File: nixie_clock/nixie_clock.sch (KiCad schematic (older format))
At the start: 1 part

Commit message: minor cleanups
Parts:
- gave numbers to parts that had none: 1
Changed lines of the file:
@@
 $EndSheet
 $Comp
-L GND #PWR?
+L GND #PWR01
 U 1 1 590D8C11
-P 3300 3050
-F 0 "#PWR?" H 3300 2800 50  0001 C CNN
-F 1 "GND" H 3300 2900 50  0000 C CNN
-F 2 "" H 3300 3050 50  0000 C CNN
-F 3 "" H 3300 3050 50  0000 C CNN
-	1    3300 3050
-	1    0    0    -1
-$EndComp
-$Comp
-L +5V #PWR?
+P 3300 3100
+F 0 "#PWR01" H 3300 2850 50  0001 C CNN
+F 1 "GND" H 3300 2950 50  0000 C CNN
+F 2 "" H 3300 3100 50  0000 C CNN
+F 3 "" H 3300 3100 50  0000 C CNN
+	1    3300 3100
+	1    0    0    -1
+$EndComp
+$Comp
+L +5V #PWR02
 U 1 1 590D8C5B
 P 3000 2700
-F 0 "#PWR?" H 3000 2550 50  0001 C CNN
+F 0 "#PWR02" H 3000 2550 50  0001 C CNN
 F 1 "+5V" H 3000 2840 50  0000 C CNN
 F 2 "" H 3000 2700 50  0000 C CNN
@@
 $EndComp
 $Comp
-L +220V #PWR?
+L +220V #PWR03
 U 1 1 5910C9E4
 P 3300 2600
-F 0 "#PWR?" H 3300 2450 50  0001 C CNN
+F 0 "#PWR03" H 3300 2450 50  0001 C CNN
 F 1 "+220V" H 3300 2740 50  0000 C CNN
 F 2 "" H 3300 2600 50  0000 C CNN
@@
 $EndSheet
 $Comp
-L +220V #PWR?
+L +220V #PWR04
 U 1 1 591129F5
 P 3300 1550
-F 0 "#PWR?" H 3300 1400 50  0001 C CNN
+F 0 "#PWR04" H 3300 1400 50  0001 C CNN
 F 1 "+220V" H 3300 1690 50  0000 C CNN
 F 2 "" H 3300 1550 50  0000 C CNN
@@
 $EndComp
 $Comp
-L +5V #PWR?
+L +5V #PWR05
 U 1 1 59112AB7
 P 2950 1700
-F 0 "#PWR?" H 2950 1550 50  0001 C CNN
+F 0 "#PWR05" H 2950 1550 50  0001 C CNN
 F 1 "+5V" H 2950 1840 50  0000 C CNN
 F 2 "" H 2950 1700 50  0000 C CNN
@@
 $EndComp
 $Comp
-L GND #PWR?
+L GND #PWR06
 U 1 1 59112B79
-P 3300 2000
-F 0 "#PWR?" H 3300 1750 50  0001 C CNN
-F 1 "GND" H 3300 1850 50  0000 C CNN
-F 2 "" H 3300 2000 50  0000 C CNN
-F 3 "" H 3300 2000 50  0000 C CNN
-	1    3300 2000
-	1    0    0    -1
-$EndComp
-$Comp
-L GND #PWR?
+P 3300 2050
+F 0 "#PWR06" H 3300 1800 50  0001 C CNN
+F 1 "GND" H 3300 1900 50  0000 C CNN
+F 2 "" H 3300 2050 50  0000 C CNN
+F 3 "" H 3300 2050 50  0000 C CNN
+	1    3300 2050
+	1    0    0    -1
+$EndComp
+$Comp
+L GND #PWR07
 U 1 1 59112C3B
 P 3300 4150
-F 0 "#PWR?" H 3300 3900 50  0001 C CNN
+F 0 "#PWR07" H 3300 3900 50  0001 C CNN
 F 1 "GND" H 3300 4000 50  0000 C CNN
 F 2 "" H 3300 4150 50  0000 C CNN
@@
 $EndComp
 $Comp
-L GND #PWR?
+L GND #PWR08
 U 1 1 59113990
 P 3100 5300
-F 0 "#PWR?" H 3100 5050 50  0001 C CNN
+F 0 "#PWR08" H 3100 5050 50  0001 C CNN
 F 1 "GND" H 3100 5150 50  0000 C CNN
 F 2 "" H 3100 5300 50  0000 C CNN
@@
 $EndComp
 $Comp
-L GND #PWR?
+L GND #PWR09
 U 1 1 59113A52
 P 3050 7150
-F 0 "#PWR?" H 3050 6900 50  0001 C CNN
+F 0 "#PWR09" H 3050 6900 50  0001 C CNN
 F 1 "GND" H 3050 7000 50  0000 C CNN
 F 2 "" H 3050 7150 50  0000 C CNN
@@
 $EndComp
 $Comp
-L +5V #PWR?
+L +5V #PWR010
 U 1 1 591147FE
 P 3000 3750
-F 0 "#PWR?" H 3000 3600 50  0001 C CNN
+F 0 "#PWR010" H 3000 3600 50  0001 C CNN
 F 1 "+5V" H 3000 3890 50  0000 C CNN
 F 2 "" H 3000 3750 50  0000 C CNN
@@
 $EndComp
 $Comp
-L +5V #PWR?
+L +5V #PWR011
 U 1 1 591148C0
 P 3000 4850
-F 0 "#PWR?" H 3000 4700 50  0001 C CNN
+F 0 "#PWR011" H 3000 4700 50  0001 C CNN
 F 1 "+5V" H 3000 4990 50  0000 C CNN
 F 2 "" H 3000 4850 50  0000 C CNN
@@
 $EndComp
 $Comp
-L +5V #PWR?
+L +5V #PWR012
 U 1 1 59115615
 P 3000 5850
-F 0 "#PWR?" H 3000 5700 50  0001 C CNN
+F 0 "#PWR012" H 3000 5700 50  0001 C CNN
 F 1 "+5V" H 3000 5990 50  0000 C CNN
 F 2 "" H 3000 5850 50  0000 C CNN
@@
 $EndComp
 $Comp
-L +5V #PWR?
+L +5V #PWR013
 U 1 1 591156D7
 P 3050 6900
-F 0 "#PWR?" H 3050 6750 50  0001 C CNN
+F 0 "#PWR013" H 3050 6750 50  0001 C CNN
 F 1 "+5V" H 3050 7040 50  0000 C CNN
 F 2 "" H 3050 6900 50  0000 C CNN
@@
 $EndComp
 $Comp
-L +220V #PWR?
+L +220V #PWR014
 U 1 1 591174D3
 P 3350 3600
-F 0 "#PWR?" H 3350 3450 50  0001 C CNN
+F 0 "#PWR014" H 3350 3450 50  0001 C CNN
 F 1 "+220V" H 3350 3740 50  0000 C CNN
 F 2 "" H 3350 3600 50  0000 C CNN
@@
 $EndComp
 $Comp
-L +220V #PWR?
+L +220V #PWR015
 U 1 1 59117595
 P 3000 4550
-F 0 "#PWR?" H 3000 4400 50  0001 C CNN
+F 0 "#PWR015" H 3000 4400 50  0001 C CNN
 F 1 "+220V" H 3000 4690 50  0000 C CNN
 F 2 "" H 3000 4550 50  0000 C CNN
@@
 $EndComp
 $Comp
-L +220V #PWR?
+L +220V #PWR016
 U 1 1 59118341
 P 2750 5650
-F 0 "#PWR?" H 2750 5500 50  0001 C CNN
+F 0 "#PWR016" H 2750 5500 50  0001 C CNN
 F 1 "+220V" H 2750 5790 50  0000 C CNN
 F 2 "" H 2750 5650 50  0000 C CNN
@@
 $EndComp
 $Comp
-L +220V #PWR?
+L +220V #PWR017
 U 1 1 59118403
 P 2800 6650
-F 0 "#PWR?" H 2800 6500 50  0001 C CNN
+F 0 "#PWR017" H 2800 6500 50  0001 C CNN
 F 1 "+220V" H 2800 6790 50  0000 C CNN
 F 2 "" H 2800 6650 50  0000 C CNN
@@
 	3450 6650 2800 6650
 $Comp
-L GND #PWR?
+L GND #PWR018
 U 1 1 5911B892
-P 3300 6150
-F 0 "#PWR?" H 3300 5900 50  0001 C CNN
-F 1 "GND" H 3300 6000 50  0000 C CNN
-F 2 "" H 3300 6150 50  0000 C CNN
-F 3 "" H 3300 6150 50  0000 C CNN
-	1    3300 6150
+P 3300 6200
+F 0 "#PWR018" H 3300 5950 50  0001 C CNN
+F 1 "GND" H 3300 6050 50  0000 C CNN
+F 2 "" H 3300 6200 50  0000 C CNN
+F 3 "" H 3300 6200 50  0000 C CNN
+	1    3300 6200
 	1    0    0    -1
 $EndComp
@@
 	3450 6150 3300 6150
 $Comp
-L CONN_01X04 P?
+L CONN_01X04 P1
 U 1 1 5911C866
 P 1850 1750
-F 0 "P?" H 1850 2000 50  0000 C CNN
+F 0 "P1" H 1850 2000 50  0000 C CNN
 F 1 "CONN_01X04" V 1950 1750 50  0000 C CNN
 F 2 "" H 1850 1750 50  0000 C CNN
@@
 $EndComp
 $Comp
-L GND #PWR?
+L GND #PWR019
 U 1 1 5910DDAF
 P 1650 2000
-F 0 "#PWR?" H 1650 1750 50  0001 C CNN
+F 0 "#PWR019" H 1650 1750 50  0001 C CNN
 F 1 "GND" H 1650 1850 50  0000 C CNN
 F 2 "" H 1650 2000 50  0000 C CNN
@@
 $EndComp
 $Comp
-L +5V #PWR?
+L +5V #PWR020
 U 1 1 5910DE73
 P 1500 1700
-F 0 "#PWR?" H 1500 1550 50  0001 C CNN
+F 0 "#PWR020" H 1500 1550 50  0001 C CNN
 F 1 "+5V" H 1500 1840 50  0000 C CNN
 F 2 "" H 1500 1700 50  0000 C CNN
@@
 $EndComp
 $Comp
-L +220V #PWR?
+L +220V #PWR021
 U 1 1 5910DF37
 P 1650 1450
-F 0 "#PWR?" H 1650 1300 50  0001 C CNN
+F 0 "#PWR021" H 1650 1300 50  0001 C CNN
 F 1 "+220V" H 1650 1590 50  0000 C CNN
 F 2 "" H 1650 1450 50  0000 C CNN
@@
 Wire Wire Line
 	2700 1850 3450 1850
+$Comp
+L PWR_FLAG #FLG022
+U 1 1 5913737C
+P 1150 1700
+F 0 "#FLG022" H 1150 1795 50  0001 C CNN
+F 1 "PWR_FLAG" H 1150 1880 50  0000 C CNN
+F 2 "" H 1150 1700 50  0000 C CNN
+F 3 "" H 1150 1700 50  0000 C CNN
+	1    1150 1700
+	1    0    0    -1
+$EndComp
+$Comp
+L PWR_FLAG #FLG023
+U 1 1 59137440
+P 1150 1400
+F 0 "#FLG023" H 1150 1495 50  0001 C CNN
+F 1 "PWR_FLAG" H 1150 1580 50  0000 C CNN
+F 2 "" H 1150 1400 50  0000 C CNN
+F 3 "" H 1150 1400 50  0000 C CNN
+	1    1150 1400
+	1    0    0    -1
+$EndComp
+Wire Wire Line
+	1150 1400 1500 1400
+Wire Wire Line
+	1500 1400 1500 1500
+Wire Wire Line
+	1500 1500 1650 1500
+Connection ~ 1650 1500
+Wire Wire Line
+	1150 1700 1150 1750
+Wire Wire Line
+	1150 1750 1550 1750
+Wire Wire Line
+	1550 1750 1550 1700
+Connection ~ 1550 1700
+Wire Wire Line
+	3300 2050 3300 2000
+Wire Wire Line
+	3300 3050 3300 3100
+Wire Wire Line
+	3300 6150 3300 6200
+$Comp
+L PWR_FLAG #FLG024
+U 1 1 5914A430
+P 1150 2000
+F 0 "#FLG024" H 1150 2095 50  0001 C CNN
+F 1 "PWR_FLAG" H 1150 2180 50  0000 C CNN
+F 2 "" H 1150 2000 50  0000 C CNN
+F 3 "" H 1150 2000 50  0000 C CNN
+	1    1150 2000
+	1    0    0    -1
+$EndComp
+Wire Wire Line
+	1650 2000 1150 2000
 $EndSCHEMATC

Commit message: Footprint associations
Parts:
- P1: footprint (none) -> Pin_Headers:Pin_Header_Straight_1x04_Pitch2.54mm
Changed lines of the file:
@@
 F 0 "P1" H 1850 2000 50  0000 C CNN
 F 1 "CONN_01X04" V 1950 1750 50  0000 C CNN
-F 2 "" H 1850 1750 50  0000 C CNN
+F 2 "Pin_Headers:Pin_Header_Straight_1x04_Pitch2.54mm" H 1850 1750 50  0001 C CNN
 F 3 "" H 1850 1750 50  0000 C CNN
 	1    1850 1750

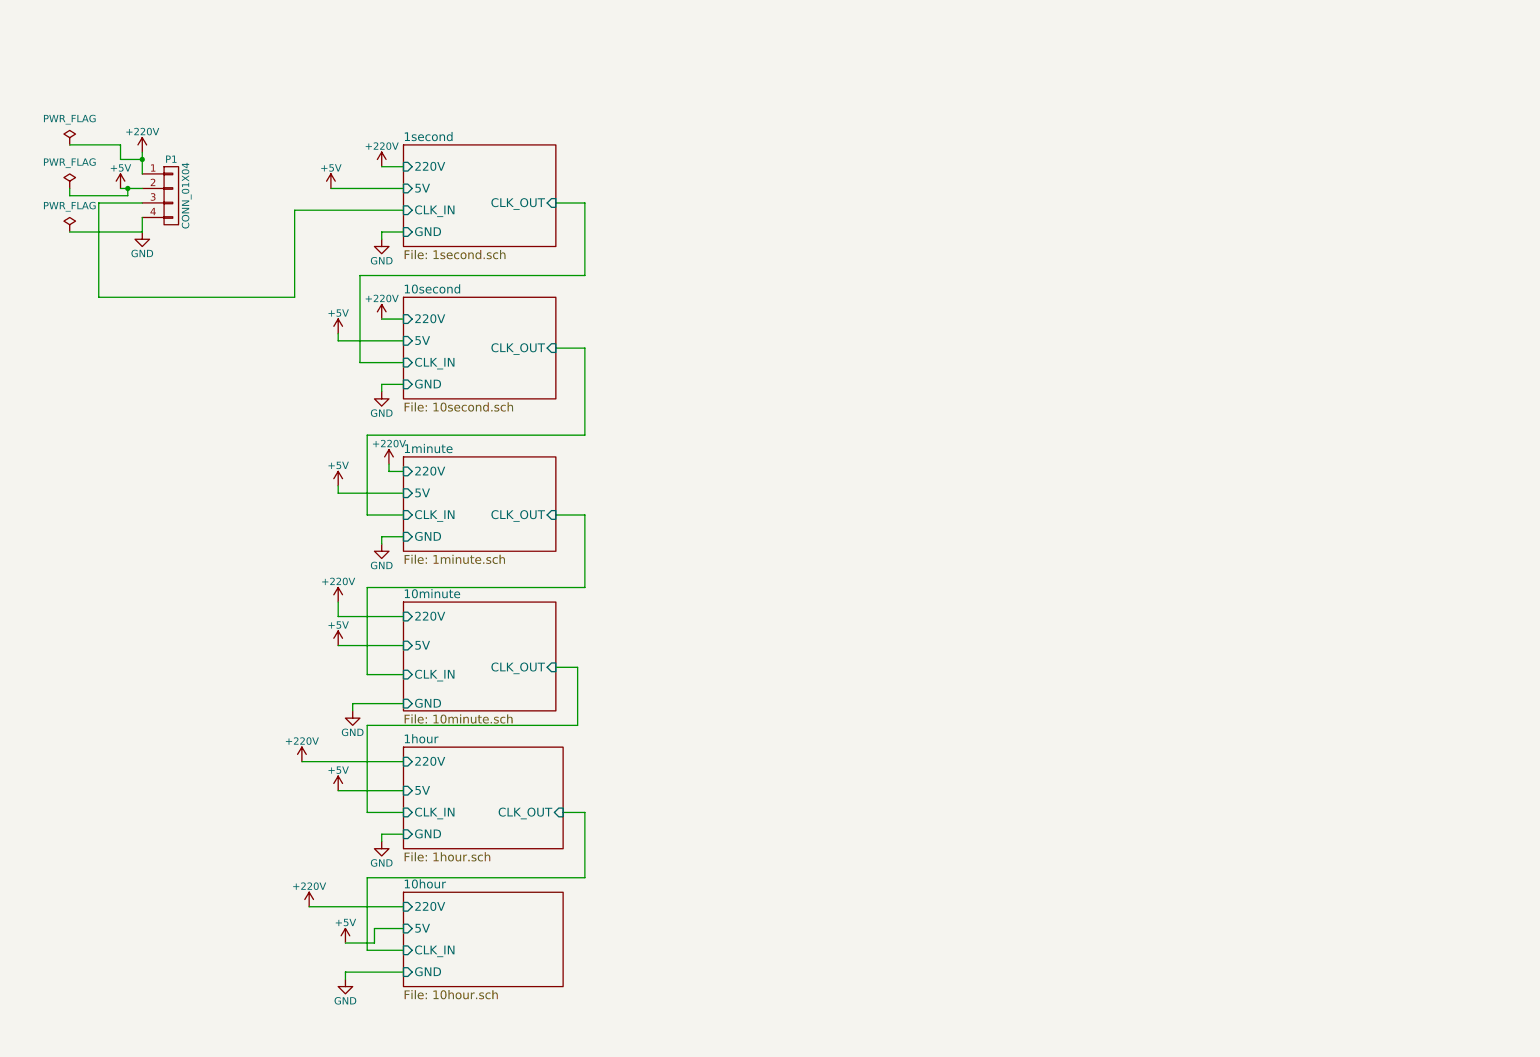
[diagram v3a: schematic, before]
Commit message: Overhaul of clock board. Fixed hour digits, added more noise immunity, reduced height
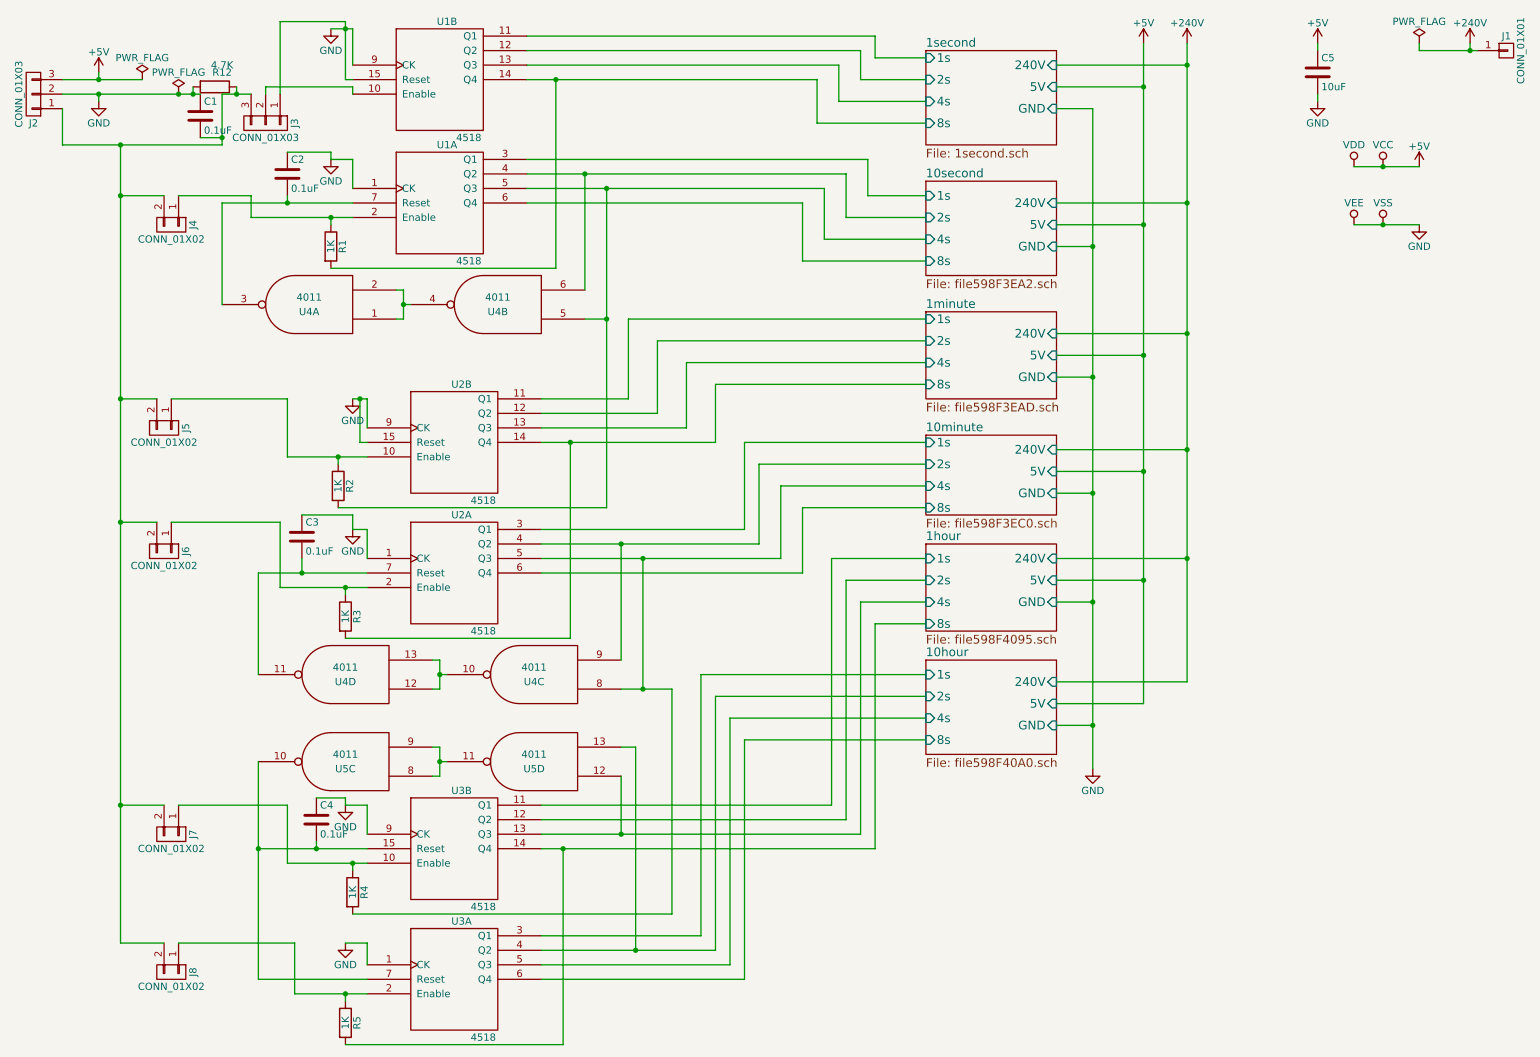
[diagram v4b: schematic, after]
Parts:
- removed P1: CONN_01X04, Pin_Headers:Pin_Header_Straight_1x04_Pitch2.54mm, symbol CONN_01X04
- added C1, C2, C3, C4: 0.1uF, Capacitors_THT:C_Axial_L5.1mm_D3.1mm_P7.50mm_Horizontal, symbol C
- added C5: 10uF, Capacitors_THT:CP_Radial_D5.0mm_P2.50mm, symbol C
- added J1: CONN_01X01, Pin_Headers:Pin_Header_Straight_1x01_Pitch2.54mm, symbol CONN_01X01
- added J2, J3: CONN_01X03, Pin_Headers:Pin_Header_Straight_1x03_Pitch2.54mm, symbol CONN_01X03
- added J4, J5, J6, J7, J8: CONN_01X02, Pin_Headers:Pin_Header_Straight_1x02_Pitch2.54mm, symbol CONN_01X02
- added R1, R2, R3, R4, R5: 1K, Resistors_THT:R_Axial_DIN0207_L6.3mm_D2.5mm_P10.16mm_Horizontal, symbol R
- added R12: 4.7K, Resistors_THT:R_Axial_DIN0207_L6.3mm_D2.5mm_P10.16mm_Horizontal, symbol R
- added U1, U2, U3: 4518, Housings_DIP:DIP-16_W7.62mm, symbol 4518
- added U4, U5: 4011, Housings_DIP:DIP-14_W7.62mm, symbol 4011
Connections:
- net +5V: now also C5.1, J2.3 (P3), U1.16 (VDD), U1.16 (VDD), U2.16 (VDD), U2.16 (VDD), U3.16 (VDD), U3.16 (VDD), U4.14 (VDD), U4.14 (VDD), U4.14 (VDD), U4.14 (VDD), U5.14 (VDD), U5.14 (VDD)
- net GND: now also C1.1, C2.1, C3.1, C4.1, C5.2, J2.2 (P2), J3.1 (P1), R12.2, U1.1 (CK), U1.15 (Reset), U1.8 (VSS), U1.8 (VSS), U1.9 (CK), U2.1 (CK), U2.15 (Reset), U2.8 (VSS), U2.8 (VSS), U2.9 (CK), U3.1 (CK), U3.8 (VSS), U3.8 (VSS), U3.9 (CK), U4.7 (VSS), U4.7 (VSS), U4.7 (VSS), U4.7 (VSS), U5.7 (VSS), U5.7 (VSS)
- new net: J3.2 (P2), U1.10 (Enable)
- new net: J4.1 (P1), R1.1, U1.2 (Enable)
- new net: C2.2, U1.7 (Reset), U4.3
- new net: J5.1 (P1), R2.1, U2.10 (Enable)
- new net: J6.1 (P1), R3.1, U2.2 (Enable)
- new net: C3.2, U2.7 (Reset), U4.11
- new net: J7.1 (P1), R4.1, U3.10 (Enable)
- new net: C4.2, U3.15 (Reset), U3.7 (Reset), U5.10
- new net: J8.1 (P1), R5.1, U3.2 (Enable)
- new net: C1.2, J2.1 (P1), J3.3 (P3), J4.2 (P2), J5.2 (P2), J6.2 (P2), J7.2 (P2), J8.2 (P2), R12.1
- new net: U4.1, U4.2, U4.4
- new net: U4.10, U4.12, U4.13
- new net: U5.11, U5.8, U5.9
- new net +240V: J1.1 (P1)
- new net 10hour/1s: U3.3 (Q1)
- new net 10hour/2s: U3.4 (Q2), U5.13
- new net 10hour/4s: U3.5 (Q3)
- new net 10hour/8s: U3.6 (Q4)
- new net 10minute/1s: U2.3 (Q1)
- new net 10minute/2s: U2.4 (Q2), U4.9
- new net 10minute/4s: R4.2, U2.5 (Q3), U4.8
- new net 10minute/8s: U2.6 (Q4)
- new net 10second/1s: U1.3 (Q1)
- new net 10second/2s: U1.4 (Q2), U4.6
- new net 10second/4s: R2.2, U1.5 (Q3), U4.5
- new net 10second/8s: U1.6 (Q4)
- new net 1hour/1s: U3.11 (Q1)
- new net 1hour/2s: U3.12 (Q2)
- new net 1hour/4s: U3.13 (Q3), U5.12
- new net 1hour/8s: R5.2, U3.14 (Q4)
- new net 1minute/1s: U2.11 (Q1)
- new net 1minute/2s: U2.12 (Q2)
- new net 1minute/4s: U2.13 (Q3)
- new net 1minute/8s: R3.2, U2.14 (Q4)
- new net 1second/1s: U1.11 (Q1)
- new net 1second/2s: U1.12 (Q2)
- new net 1second/4s: U1.13 (Q3)
- new net 1second/8s: R1.2, U1.14 (Q4)
